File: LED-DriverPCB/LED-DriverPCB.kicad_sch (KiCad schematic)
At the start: 1 part, among them U1 STM32F103RCTx

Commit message: Finished MCU connections
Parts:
- added C1, C2: C, symbol Device:C
- added C10, C3, C4, C5, C6, C7, C8: 100n, symbol Device:C
- added C9: 10u, symbol Device:C
- added J1, J2, J3, J4, J5, J6, J7, J8: Screw_Terminal_01x03, symbol Connector:Screw_Terminal_01x03
- added J10, J9: USB_C_Receptacle_USB2.0_16P, symbol Connector:USB_C_Receptacle_USB2.0_16P
- added J11: AudioJack2_Ground, symbol Connector_Audio:AudioJack2_Ground
- added J12, J13, J14, J15, J16, J17, J18, J19: Screw_Terminal_01x02, symbol Connector:Screw_Terminal_01x02
- added J20: Conn_ARM_SWD_TagConnect_TC2030, Connector:Tag-Connect_TC2030-IDC-FP_2x03_P1.27mm_Vertical, symbol Connector:Conn_ARM_SWD_TagConnect_TC2030
- added R1: 10k, symbol Device:R
- added R2, R3: 5.1k, symbol Device:R
- added SW1: SW_SPDT, symbol Switch:SW_SPDT
- added U2: PCM2704C, symbol LED-Driver_SymbolLib:PCM2704C
- added U3: AMS1117-3.3, Package_TO_SOT_SMD:SOT-223-3_TabPin2, symbol Regulator_Linear:AMS1117-3.3
- added U4: USBLC6-2SC6, Package_TO_SOT_SMD:SOT-23-6, symbol Power_Protection:USBLC6-2SC6
- added X1: 8MHz, symbol Device:Crystal_GND24
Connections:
- net +3.3V: now reaches U1.1 (VBAT)
- net +3.3V: now also U1.13 (VDDA), U1.19 (VDD), U1.32 (VDD), U1.48 (VDD), U1.64 (VDD), C3.1, C4.1, C5.1, C6.1, C7.1, C8.1, C9.1, J20.1 (VCC), SW1.3 (C)
- net GND: now reaches U1.12 (VSSA)
- net GND: now also U1.18 (VSS), U1.31 (VSS), U1.47 (VSS), U1.63 (VSS), C1.2, C10.2, C2.2, C3.2, C4.2, C5.2, C6.2, C7.2, C8.2, C9.2, J20.5 (GND), J9.A1 (GND), J9.A12 (GND), J9.B1 (GND), J9.B12 (GND), J9.S1 (SHIELD), R2.1, R3.1, SW1.1 (A), U4.2 (GND), X1.2, X1.4
- net PWM_TIM5_CH1: now reaches U1.14 (PA0)
- net PWM_TIM5_CH2: now reaches U1.15 (PA1)
- net PWM_TIM5_CH3: now reaches U1.16 (PA2)
- net PWM_TIM5_CH4: now reaches U1.17 (PA3)
- net PWM_TIM3_CH1: now reaches U1.22 (PA6)
- net PWM_TIM8_CH1: now reaches U1.25 (PC5)
- net PWM_TIM3_CH3: now reaches U1.26 (PB0)
- net PWM_TIM3_CH4: now reaches U1.27 (PB1)
- net USB_CON_D-: now reaches U1.44 (PA11)
- net USB_CON_D-: now also J9.A7 (D-), J9.B7 (D-), U4.1 (I/O1), U4.6 (I/O1)
- net USB_CON_D+: now reaches U1.45 (PA12)
- net USB_CON_D+: now also J9.A6 (D+), J9.B6 (D+), U4.3 (I/O2), U4.4 (I/O2)
- net SWD_DIO: now reaches U1.46 (PA13)
- net SWD_DIO: now also J20.2 (SWDIO)
- net SWD_CLK: now reaches U1.49 (PA14)
- net SWD_CLK: now also J20.4 (SWCLK)
- net HSE_IN: now reaches U1.5 (PD0)
- net HSE_IN: now also C1.1, X1.1
- net SWD_SWO: now reaches U1.55 (PB3)
- net SWD_SWO: now also J20.6 (SWO)
- net HSE_OUT: now reaches U1.6 (PD1)
- net HSE_OUT: now also C2.1, X1.3
- net BOOT: now reaches U1.60 (BOOT0)
- net BOOT: now also R1.2
- net SWD_NRST: now reaches U1.7 (NRST)
- net SWD_NRST: now also C10.1, J20.3 (~{RESET})
- new net: J10.A1 (GND), J10.A12 (GND), J10.B1 (GND), J10.B12 (GND)
- new net: J10.A4 (VBUS), J10.A9 (VBUS), J10.B4 (VBUS), J10.B9 (VBUS)
- new net SW_BOOT: R1.1, SW1.2 (B)
- new net USB_CC1: J9.A5 (CC1), R2.2
- new net USB_CC2: J9.B5 (CC2), R3.2
- new net VBUS: J9.A4 (VBUS), J9.A9 (VBUS), J9.B4 (VBUS), J9.B9 (VBUS), U4.5 (VBUS)
- no-connect marks 0 -> 2
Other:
- moved on the sheet: U1

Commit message: Finished schematic
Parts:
- removed J10: USB_C_Receptacle_USB2.0_16P, symbol Connector:USB_C_Receptacle_USB2.0_16P
- removed J11: AudioJack2_Ground, symbol Connector_Audio:AudioJack2_Ground
- removed U2: PCM2704C, symbol LED-Driver_SymbolLib:PCM2704C
- added C11: 10u, symbol Device:C_Polarized
- added C12: 22u, symbol Device:C_Polarized
- added C13, C14: 0.1u, symbol Device:C
- added C15: 10u, symbol Device:C
- added R4: 50k, symbol Device:R
- added R5: 1.5k, symbol Device:R
- added U2: TXB0108PW, Package_SO:TSSOP-20_4.4x6.5mm_P0.65mm, symbol Logic_LevelTranslator:TXB0108PW
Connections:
- net +3.3V: now also U3.2 (VO), C12.1, C13.1, R4.1, R5.1, U2.2 (V_{CCA})
- net GND: now also J1.3 (Pin_3), J12.2 (Pin_2), J13.2 (Pin_2), J14.2 (Pin_2), J15.2 (Pin_2), J16.2 (Pin_2), J17.2 (Pin_2), J18.2 (Pin_2), J19.2 (Pin_2), J2.3 (Pin_3), J3.3 (Pin_3), J4.3 (Pin_3), J5.3 (Pin_3), J6.3 (Pin_3), J7.3 (Pin_3), J8.3 (Pin_3), U3.1 (GND), C11.2, C12.2, C13.2, C14.2, C15.2, U2.11 (GND)
- net PWM_TIM3_CH1: now also U2.6 (A5)
- net PWM_TIM3_CH3: now also U2.8 (A7)
- net PWM_TIM5_CH1: now also U2.1 (A1)
- net PWM_TIM5_CH2: now also U2.3 (A2)
- net PWM_TIM5_CH3: now also U2.4 (A3)
- net PWM_TIM5_CH4: now also U2.5 (A4)
- net PWM_TIM8_CH1: now also U2.9 (A8)
- net USB_CON_D+: now also R5.2
- net VBUS: now also U3.3 (VI), C11.1
- net STR5_PWR: now reaches J16.1 (Pin_1)
- net STR5_PWR: now also J5.1 (Pin_1)
- net STR2_PWR: now reaches J13.1 (Pin_1)
- net STR2_PWR: now also J2.1 (Pin_1)
- net STR8_PWR: now reaches J19.1 (Pin_1)
- net STR8_PWR: now also J8.1 (Pin_1)
- net STR1_PWR: now reaches J1.1 (Pin_1)
- net STR1_PWR: now also J12.1 (Pin_1)
- net STR1_DATA: now reaches J1.2 (Pin_2)
- net STR1_DATA: now also U2.20 (B1)
- net STR4_PWR: now reaches J15.1 (Pin_1)
- net STR4_PWR: now also J4.1 (Pin_1)
- net STR4_DATA: now reaches J4.2 (Pin_2)
- net STR4_DATA: now also U2.16 (B4)
- net STR6_PWR: now reaches J6.1 (Pin_1)
- net STR6_PWR: now also J17.1 (Pin_1)
- net STR6_DATA: now reaches J6.2 (Pin_2)
- net STR6_DATA: now also U2.14 (B6)
- net STR7_PWR: now reaches J18.1 (Pin_1)
- net STR7_PWR: now also J7.1 (Pin_1)
- net STR8_DATA: now reaches J8.2 (Pin_2)
- net STR8_DATA: now also U2.12 (B8)
- net STR5_DATA: now reaches J5.2 (Pin_2)
- net STR5_DATA: now also U2.15 (B5)
- net STR2_DATA: now reaches J2.2 (Pin_2)
- net STR2_DATA: now also U2.18 (B2)
- net STR7_DATA: now reaches J7.2 (Pin_2)
- net STR7_DATA: now also U2.13 (B7)
- net STR3_PWR: now reaches J14.1 (Pin_1)
- net STR3_PWR: now also J3.1 (Pin_1)
- net STR3_DATA: now reaches J3.2 (Pin_2)
- net STR3_DATA: now also U2.17 (B3)
- new net: R4.2, U2.10 (OE)
- new net +5V: C14.1, C15.1, U2.19 (V_{CCB})
- new net PWM_TIM3_CH2: U2.7 (A6)
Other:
- note added: "**DOUBLE CHECK CONNECTOR ORIENTATION**"
- note added: "*Pick crystal park to get load capacitances"
- note added: "*Tantalum capacitors"
- moved on the sheet: J1, J12, J13, J14, J15, J16, J17, J18, J19, J2, J3, J4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

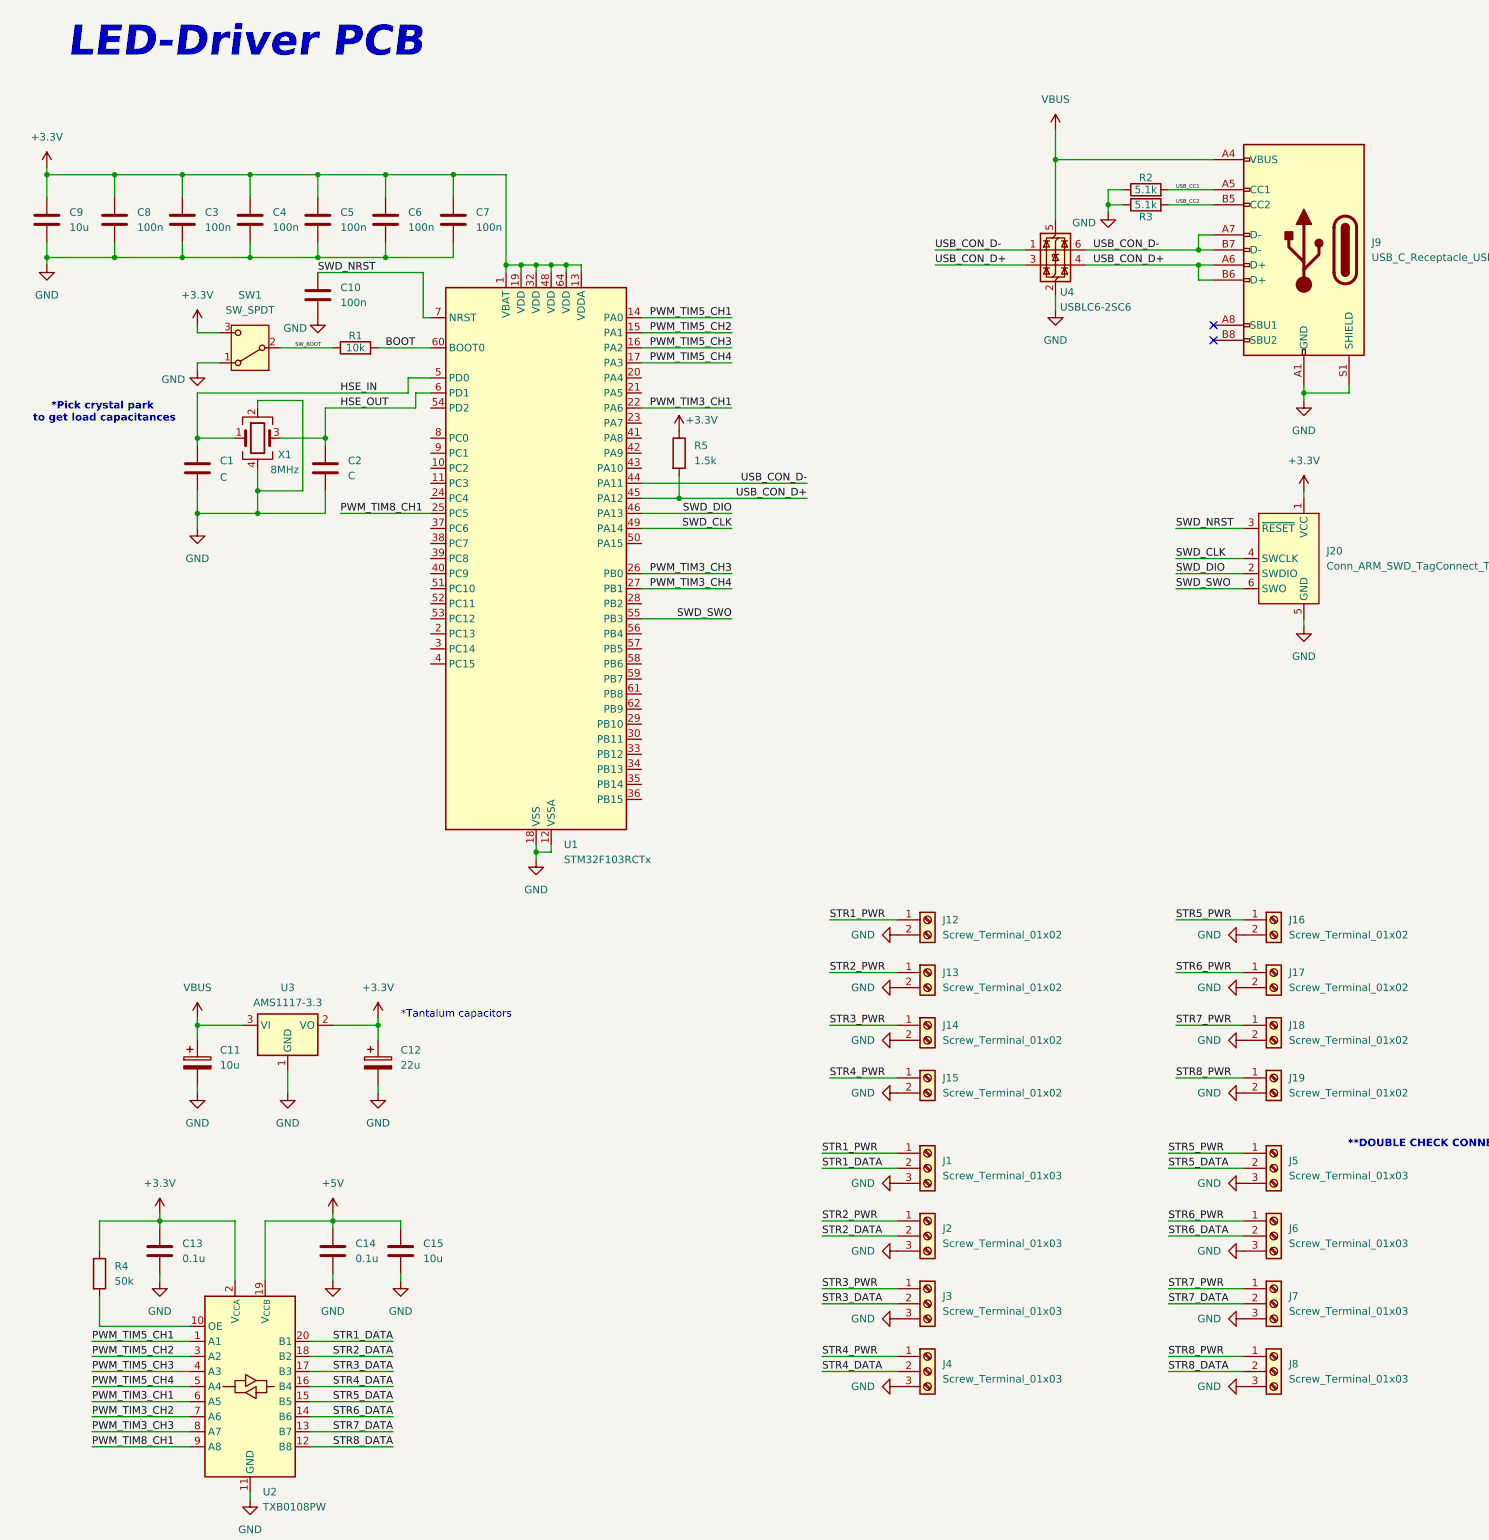
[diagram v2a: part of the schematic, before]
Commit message: Added footprints
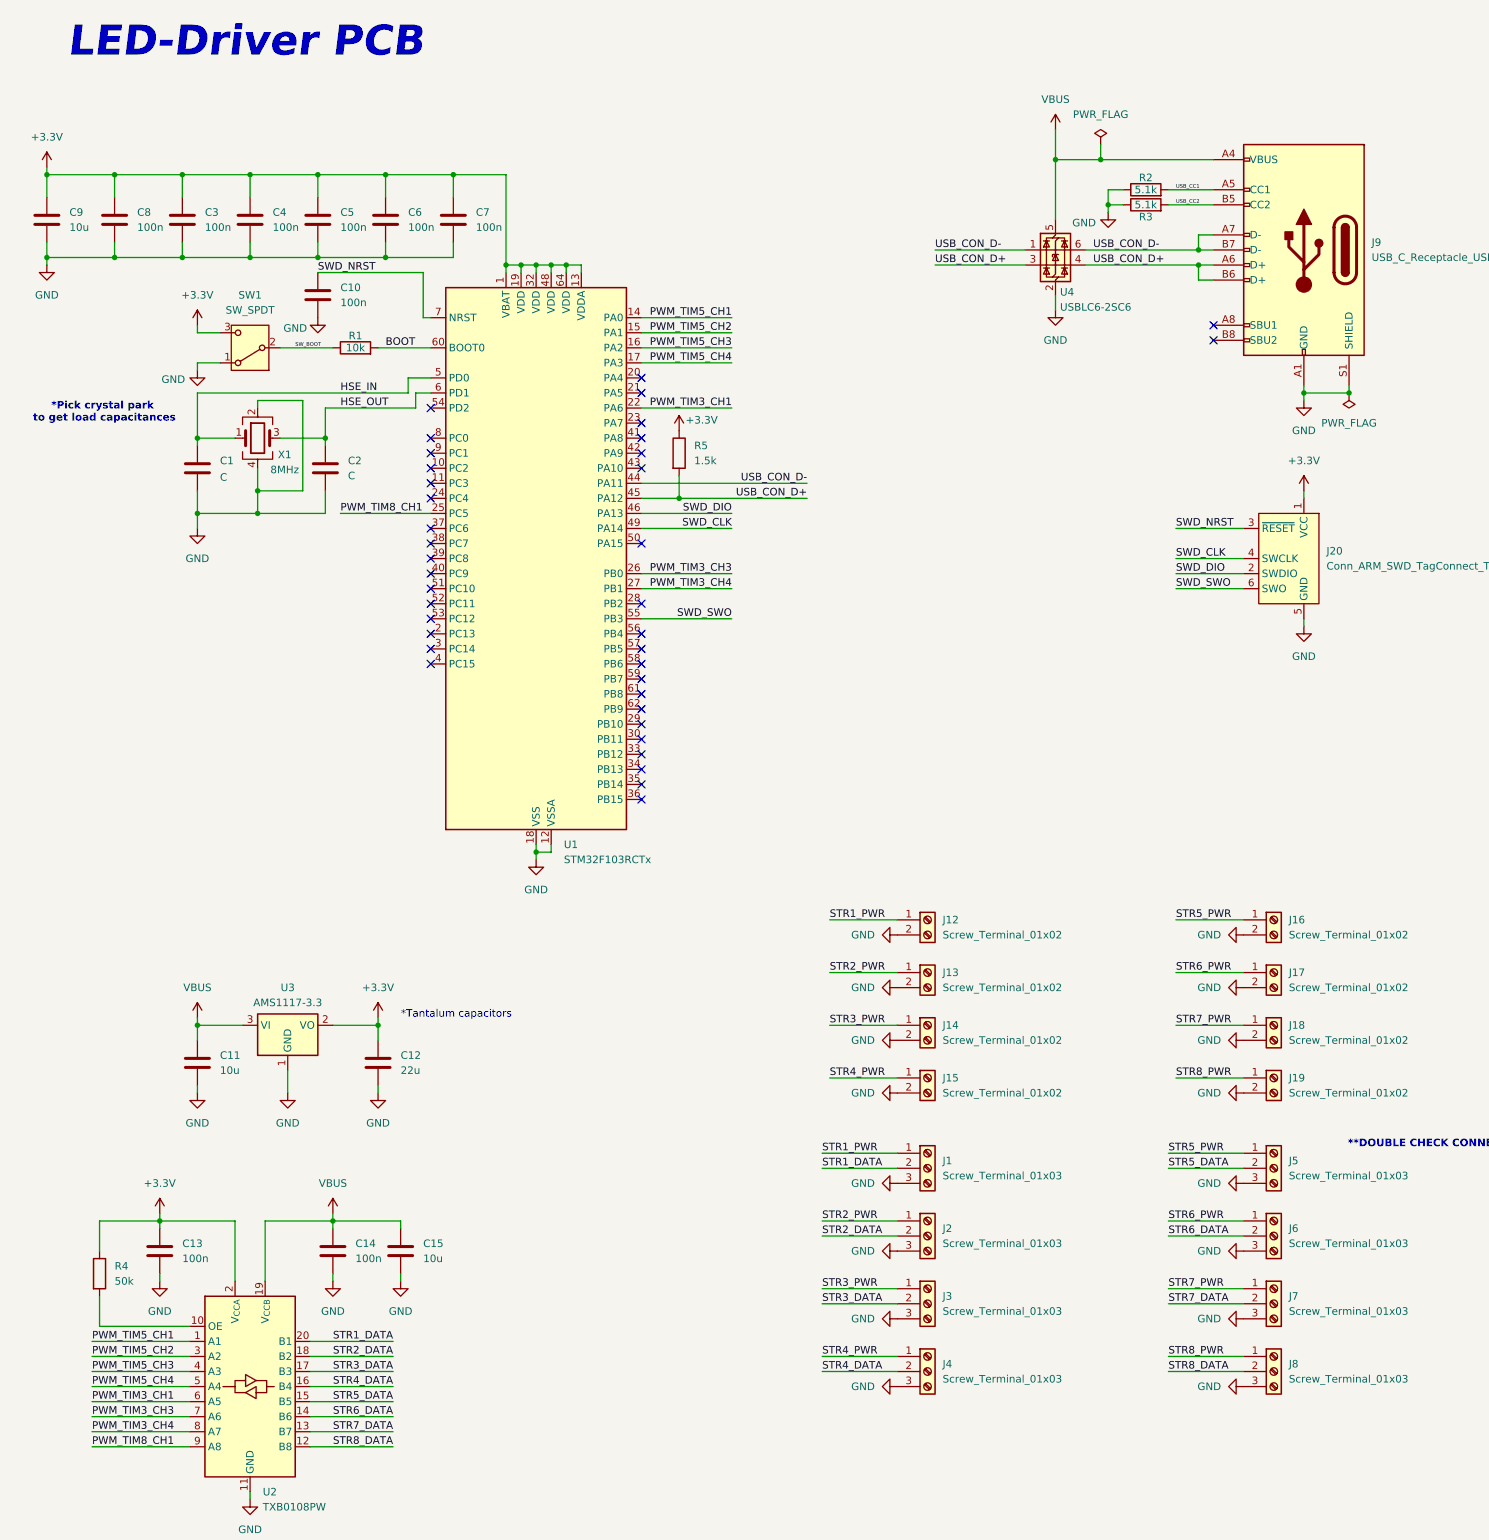
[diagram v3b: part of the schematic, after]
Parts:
- removed C11: 10u, symbol Device:C_Polarized
- removed C12: 22u, symbol Device:C_Polarized
- added C11: 10u, Capacitor_SMD:C_0805_2012Metric, symbol Device:C
- added C12: 22u, Capacitor_SMD:C_0805_2012Metric, symbol Device:C
- C1, C2: footprint (none) -> Capacitor_SMD:C_0402_1005Metric
- C10, C3, C4, C5, C6, C7, C8: footprint (none) -> Capacitor_SMD:C_0603_1608Metric
- C13, C14: value 0.1u -> 100n; footprint (none) -> Capacitor_SMD:C_0603_1608Metric
- C15, C9: footprint (none) -> Capacitor_SMD:C_0805_2012Metric
- J1, J2, J3, J4, J5, J6, J7, J8: footprint (none) -> 39303037:CONN_5569-03A4&slash_5_MOL
- J12, J13, J14, J15, J16, J17, J18, J19: footprint (none) -> 26013114:CONN_5569-02A_MOL
- J9: footprint (none) -> Connector_USB:USB_C_Receptacle_HRO_TYPE-C-31-M-12
- R1, R2, R3, R4, R5: footprint (none) -> Resistor_SMD:R_0603_1608Metric
- SW1: footprint (none) -> Button_Switch_SMD:SW_SPDT_PCM12
- X1: footprint (none) -> Crystal:Crystal_SMD_3225-4Pin_3.2x2.5mm
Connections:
- net +5V is gone; now on net VBUS: C14.1, C15.1, U2.19 (V_{CCB})
- net PWM_TIM3_CH2 is gone; now on net PWM_TIM3_CH3: U2.7 (A6)
- net +3.3V: now also C12.1
- net GND: now also C11.2, C12.2
- net PWM_TIM3_CH3: no longer U2.8 (A7)
- net PWM_TIM3_CH4: now also U2.8 (A7)
- net VBUS: now also C11.1
- no-connect marks 2 -> 38
